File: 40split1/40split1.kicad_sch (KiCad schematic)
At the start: 46 parts, among them U1 Raspberry_Pi_Pico, U2 TRRS

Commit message: sorted out trrs
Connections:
- net Tip: now also U1.39 (VSYS); no longer U1.4 (GPIO2)
- net sleeve: now also U1.42 (GND); no longer U1.7 (GPIO5)
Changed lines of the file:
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@@
-	(wire
-		(pts
-			(xy 224.79 62.23) (xy 222.25 62.23)
-		)
-		(stroke
-			(width 0)
-			(type default)
-		)
-	)
 	(wire
 		(pts
@@
 	(wire
 		(pts
+			(xy 240.03 100.33) (xy 240.03 102.87)
+		)
+		(stroke
+			(width 0)
+			(type default)
+		)
+	)
+	(wire
+		(pts
 			(xy 146.05 85.09) (xy 146.05 101.6)
 		)
@@
 	(wire
 		(pts
-			(xy 224.79 54.61) (xy 222.25 54.61)
-		)
-		(stroke
-			(width 0)
-			(type default)
-		)
-	)
-	(wire
-		(pts
 			(xy 125.73 81.28) (xy 138.43 81.28)
 		)
@@
 	(wire
 		(pts
+			(xy 255.27 49.53) (xy 259.08 49.53)
+		)
+		(stroke
+			(width 0)
+			(type default)
+		)
+	)
+	(wire
+		(pts
 			(xy 176.53 114.3) (xy 189.23 114.3)
 		)
@@
 	(global_label "sleeve"
 		(shape input)
-		(at 222.25 62.23 180)
+		(at 240.03 102.87 270)
 		(fields_autoplaced yes)
 		(effects
@@
 		)
 		(property "Intersheetrefs" "${INTERSHEET_REFS}"
-			(at 213.3381 62.23 0)
+			(at 240.03 111.7819 90)
 			(effects
 				(font
@@
 	(global_label "Tip"
 		(shape input)
-		(at 222.25 54.61 180)
-		(fields_autoplaced yes)
-		(effects
-			(font
-				(size 1.27 1.27)
-			)
-			(justify right)
-		)
-		(property "Intersheetrefs" "${INTERSHEET_REFS}"
-			(at 216.5434 54.61 0)
-			(effects
-				(font
-					(size 1.27 1.27)
-				)
-				(justify right)
-				(hide yes)
-			)
+		(at 259.08 49.53 0)
+		(fields_autoplaced yes)
+		(effects
+			(font
+				(size 1.27 1.27)
+			)
+			(justify left)
+		)
+		(property "Intersheetrefs" "${INTERSHEET_REFS}"
+			(at 264.7866 49.53 0)
+			(effects
+				(font
+					(size 1.27 1.27)
+				)
+				(justify left)
+				(hide yes)
+			)

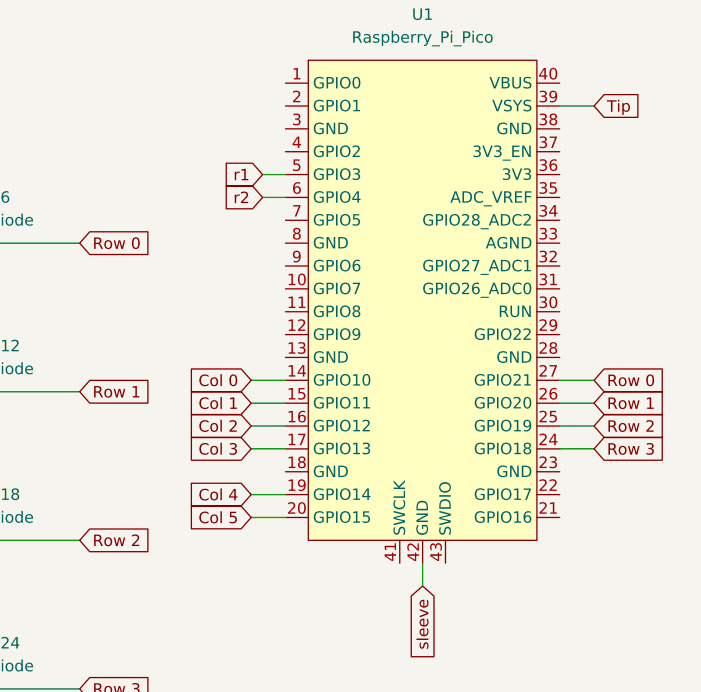
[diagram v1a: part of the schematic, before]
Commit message: adjusted schematics a little, finished all routing
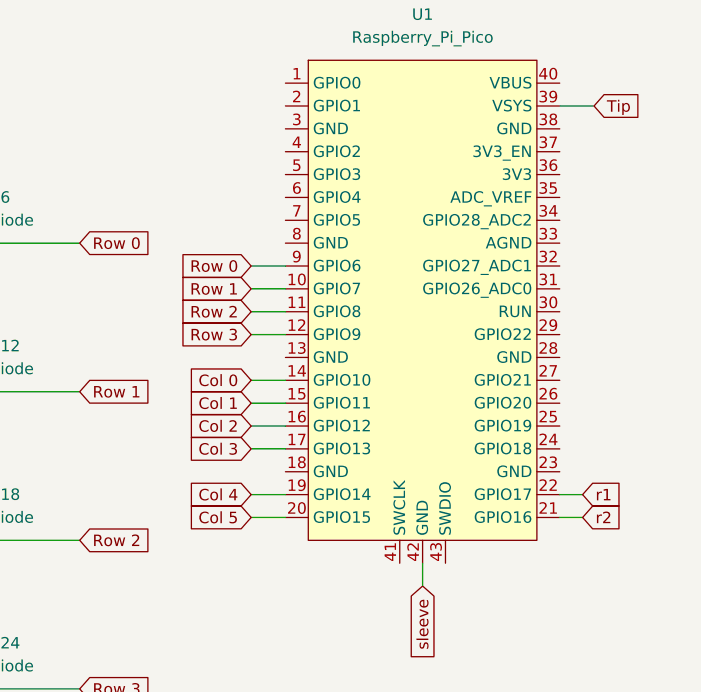
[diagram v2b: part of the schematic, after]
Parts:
- S24: footprint ScottoKeebs_MX:MX_PCB_1.00u -> ScottoKeebs_MX:MX_PCB_1.50u
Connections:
- net Row 0: now also U1.9 (GPIO6); no longer U1.27 (GPIO21)
- net Row 1: now also U1.10 (GPIO7); no longer U1.26 (GPIO20)
- net Row 2: now also U1.11 (GPIO8); no longer U1.25 (GPIO19)
- net Row 3: now also U1.12 (GPIO9); no longer U1.24 (GPIO18)
- net r1: now also U1.22 (GPIO17); no longer U1.5 (GPIO3)
- net r2: now also U1.21 (GPIO16); no longer U1.6 (GPIO4)
